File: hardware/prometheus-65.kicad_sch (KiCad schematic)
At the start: 3 parts, among them J1 Conn_01x04_Socket, U1 STM32F405RGTx, U2 TMUX1308

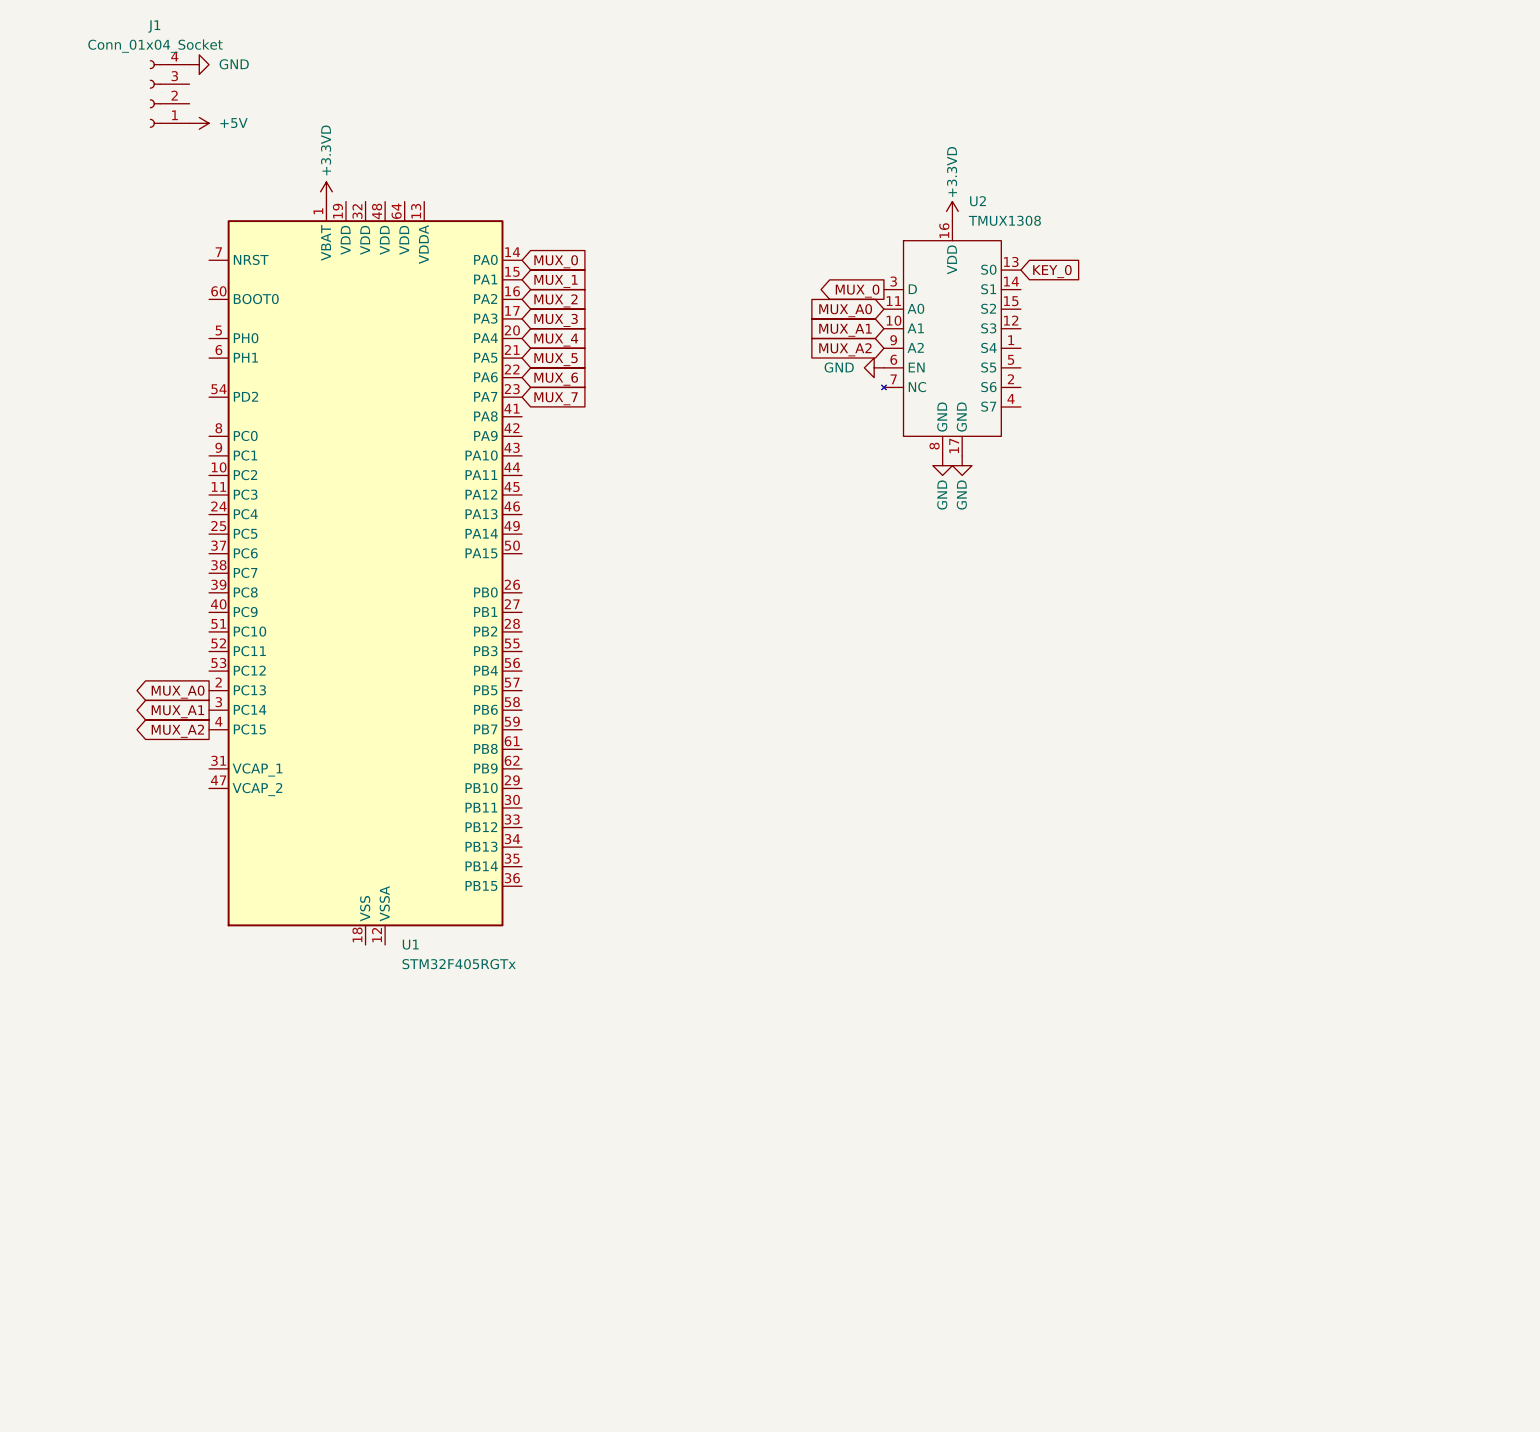
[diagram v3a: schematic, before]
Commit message: feat: added power, clock, usb header, and SWD circuits to STM32, added symbol, footprint, and 3d model for TPS7A47000RGWT from SnapEda
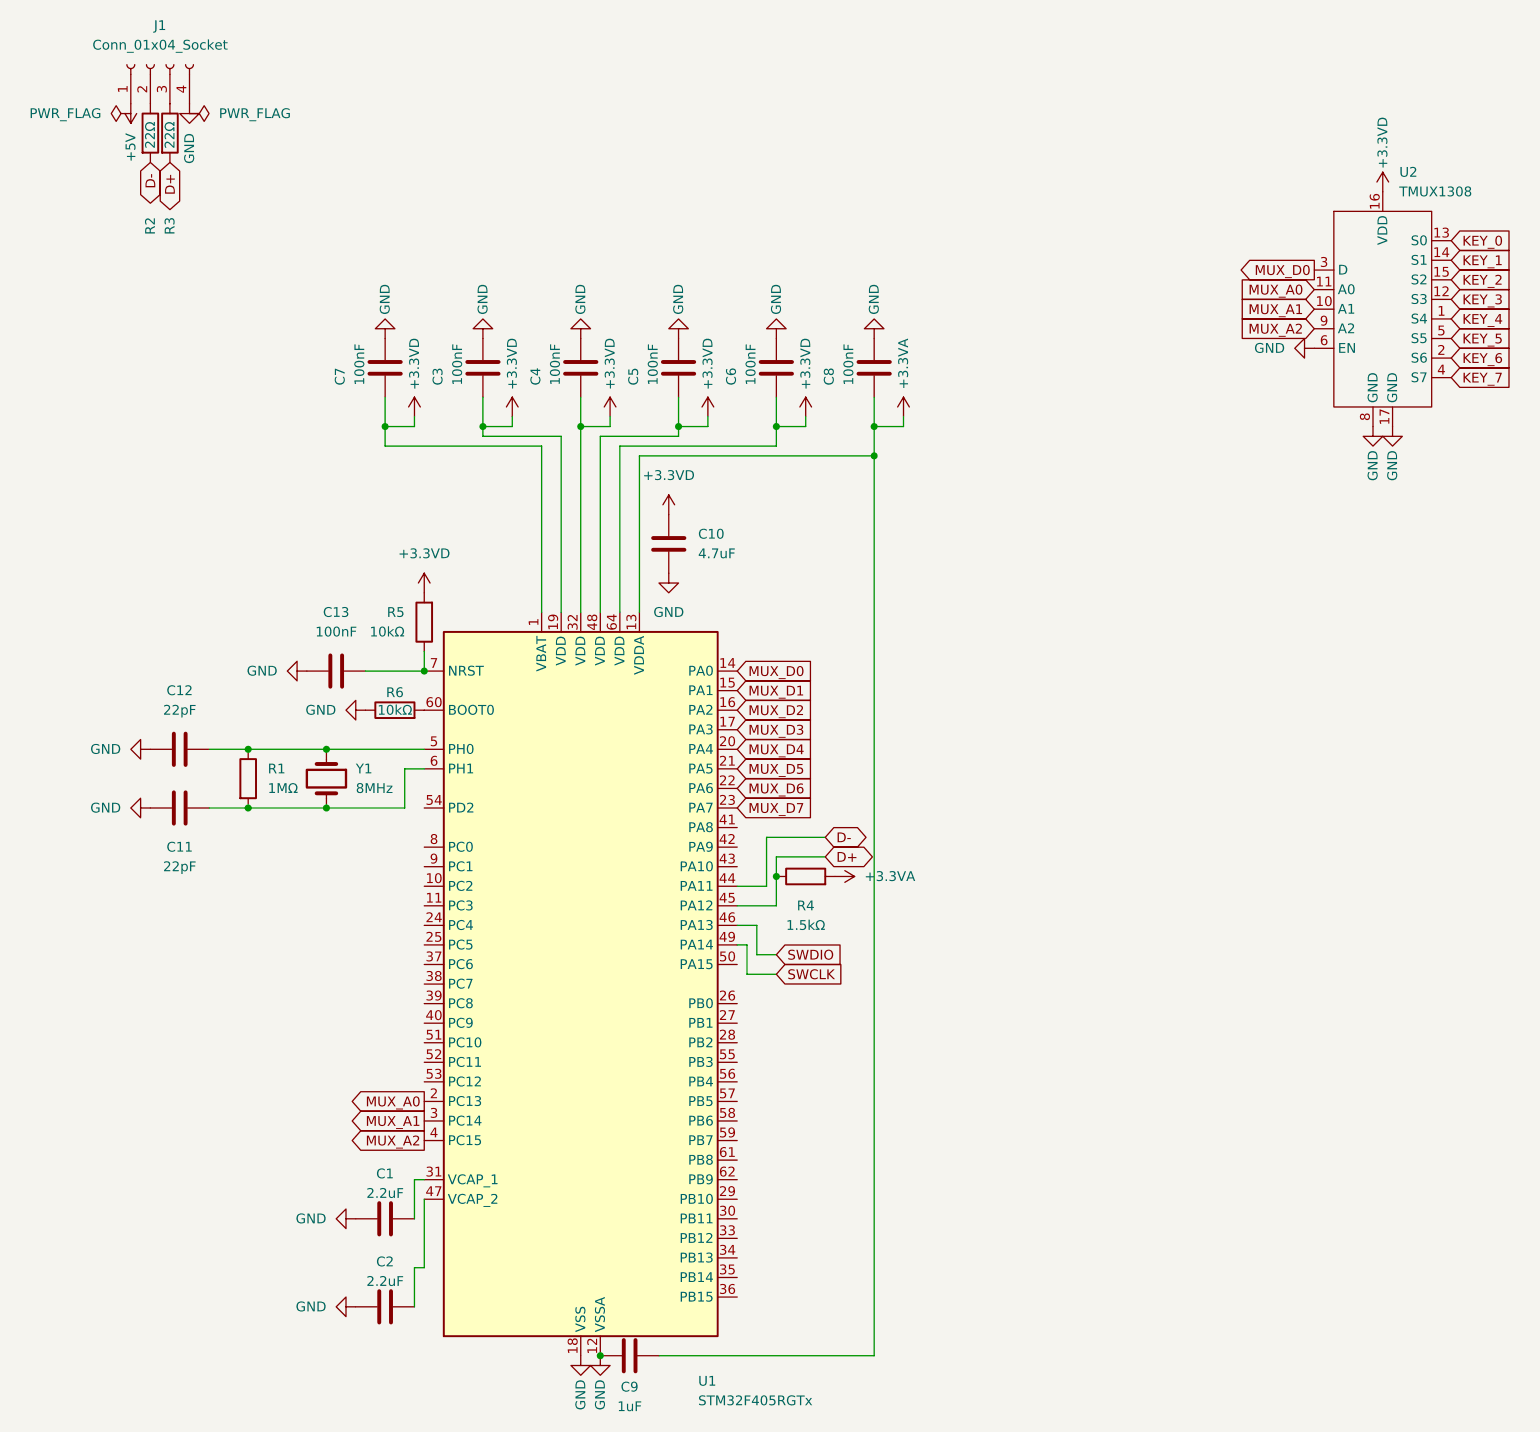
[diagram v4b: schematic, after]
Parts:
- added C1, C2: 2.2uF, symbol Device:C
- added C10: 4.7uF, symbol Device:C
- added C11, C12: 22pF, symbol Device:C
- added C13, C3, C4, C5, C6, C7, C8: 100nF, symbol Device:C
- added C9: 1uF, symbol Device:C
- added R1: 1MΩ, symbol Device:R
- added R2, R3: 22Ω, symbol Device:R
- added R4: 1.5kΩ, symbol Device:R
- added R5, R6: 10kΩ, symbol Device:R
- added Y1: 8MHz, symbol Device:Crystal
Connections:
- net +3.3VD: now also U1.19 (VDD), U1.32 (VDD), U1.48 (VDD), U1.64 (VDD), C10.1, C3.2, C4.2, C5.2, C6.2, C7.2, R5.2
- net GND: now also U1.12 (VSSA), U1.18 (VSS), U1.63 (VSS), C1.1, C10.2, C11.1, C12.1, C13.1, C2.1, C3.1, C4.1, C5.1, C6.1, C7.1, C8.1, C9.1, R6.1
- net +3.3VA: now reaches U1.13 (VDDA)
- net +3.3VA: now also C8.2, C9.2, R4.2
- net at U1.31 (VCAP_1): now also C1.2
- net D-: now reaches U1.44 (PA11)
- net D-: now also R2.2
- net D+: now reaches U1.45 (PA12)
- net D+: now also R3.2, R4.1
- net SWDIO: now reaches U1.46 (PA13)
- net at U1.47 (VCAP_2): now also C2.2
- net SWCLK: now reaches U1.49 (PA14)
- net at U1.5 (PH0): now also C12.2, R1.1, Y1.1
- net at U1.6 (PH1): now also C11.2, R1.2, Y1.2
- net at U1.60 (BOOT0): now also R6.2
- net at U1.7 (NRST): now also C13.2, R5.1
- net at J1.2 (Pin_2): now also R2.1
- net at J1.3 (Pin_3): now also R3.1
- net KEY_4: now reaches U2.1 (S4)
- net KEY_3: now reaches U2.12 (S3)
- net KEY_1: now reaches U2.14 (S1)
- net KEY_2: now reaches U2.15 (S2)
- net KEY_6: now reaches U2.2 (S6)
- net KEY_7: now reaches U2.4 (S7)
- net KEY_5: now reaches U2.5 (S5)
- net MUX_0 renamed MUX_D0
- net MUX_1 renamed MUX_D1
- net MUX_2 renamed MUX_D2
- net MUX_3 renamed MUX_D3
- net MUX_4 renamed MUX_D4
- net MUX_5 renamed MUX_D5
- net MUX_6 renamed MUX_D6
- net MUX_7 renamed MUX_D7
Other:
- moved on the sheet: J1, U1
